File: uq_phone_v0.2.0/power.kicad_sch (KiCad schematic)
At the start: 37 parts, among them J2 124018312112A, J3 BM03B-ACHSS-GAN-TF_LF__SN_, U1 TPS62162DSGR, U15 TPS22964CYZPR, U2 MCP73871-2CCI_ML, U3 BQ27441DRZR-G1A

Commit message: Restructure, route and add flex pcb
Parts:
- C1, C3: LCSC PN C2168196 -> C19702
- C5: LCSC PN C26412 -> C526993
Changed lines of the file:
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@@
 			)
 		)
-		(property "LCSC PN" "C26412"
+		(property "LCSC PN" "C526993"
 			(at 273.05 185.42 0)
 			(effects
@@
 			)
 		)
-		(property "LCSC PN" "C2168196"
+		(property "LCSC PN" "C19702"
 			(at 90.17 173.99 0)
 			(effects
@@
 			)
 		)
-		(property "LCSC PN" "C2168196"
+		(property "LCSC PN" "C19702"
 			(at 213.36 59.69 0)
 			(effects

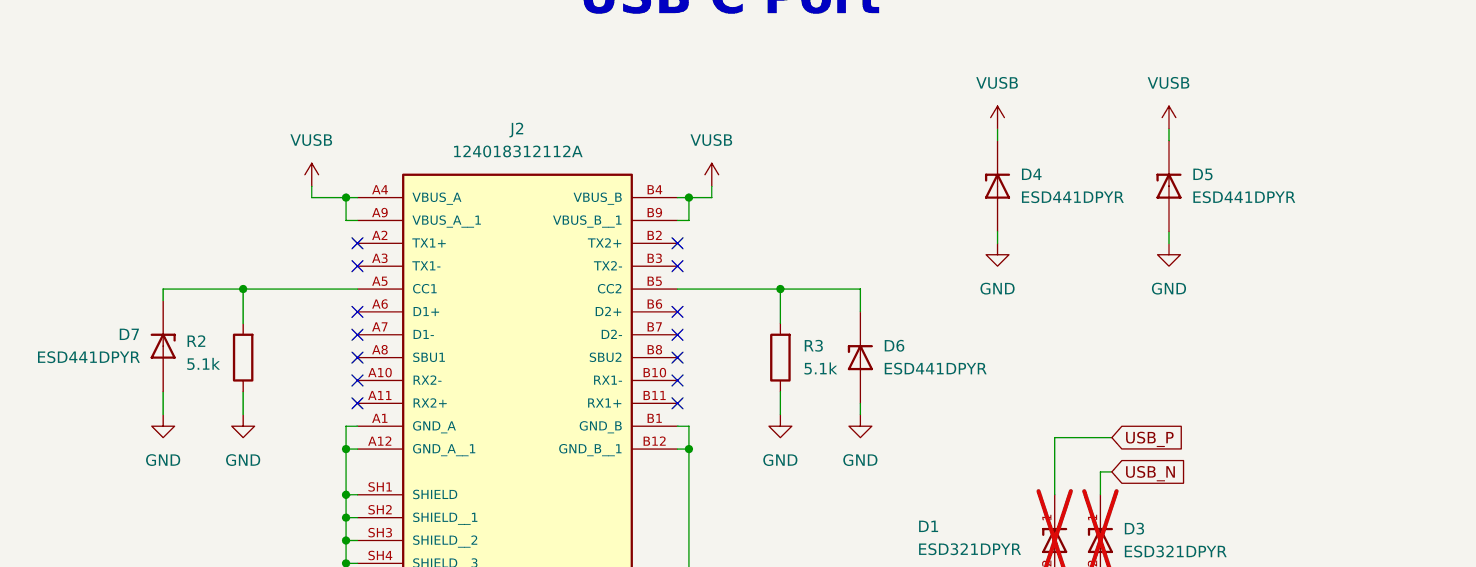
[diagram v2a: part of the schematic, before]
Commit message: Add GNSS antenna for sag
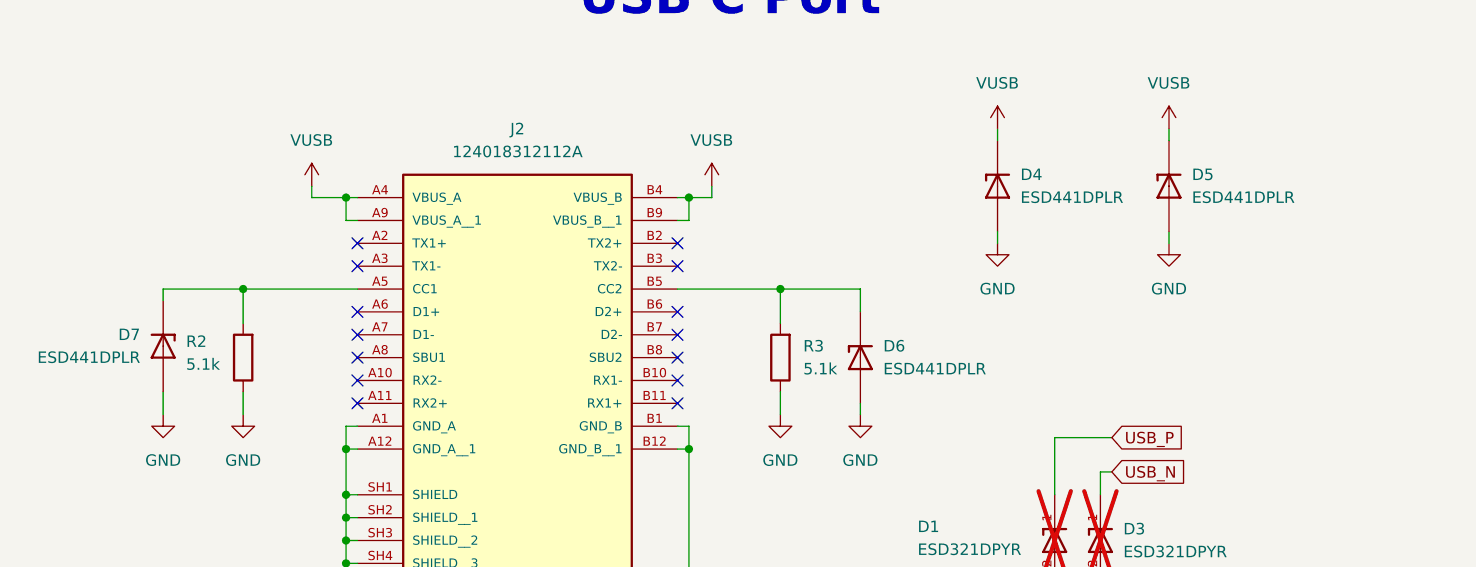
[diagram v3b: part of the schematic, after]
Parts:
- D4, D5, D6, D7: value ESD441DPYR -> ESD441DPLR
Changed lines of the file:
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@@
 			)
 		)
-		(property "Value" "ESD441DPYR"
+		(property "Value" "ESD441DPLR"
 			(at 124.46 43.1799 90)
 			(effects
@@
 			)
 		)
-		(property "Value" "ESD441DPYR"
+		(property "Value" "ESD441DPLR"
 			(at 109.22 62.2299 90)
 			(effects
@@
 			)
 		)
-		(property "Value" "ESD441DPYR"
+		(property "Value" "ESD441DPLR"
 			(at 143.51 43.1799 90)
 			(effects
@@
 			)
 		)
-		(property "Value" "ESD441DPYR"
+		(property "Value" "ESD441DPLR"
 			(at 26.67 60.9599 90)
 			(effects

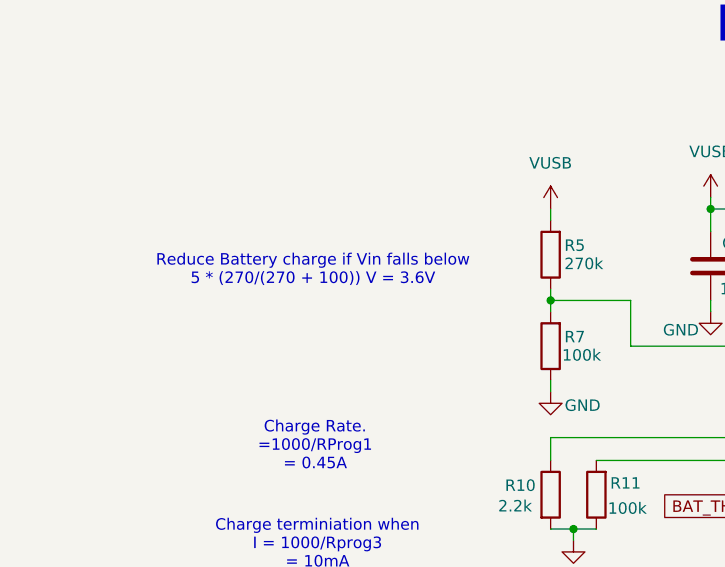
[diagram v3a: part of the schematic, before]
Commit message: Fixed display pinout
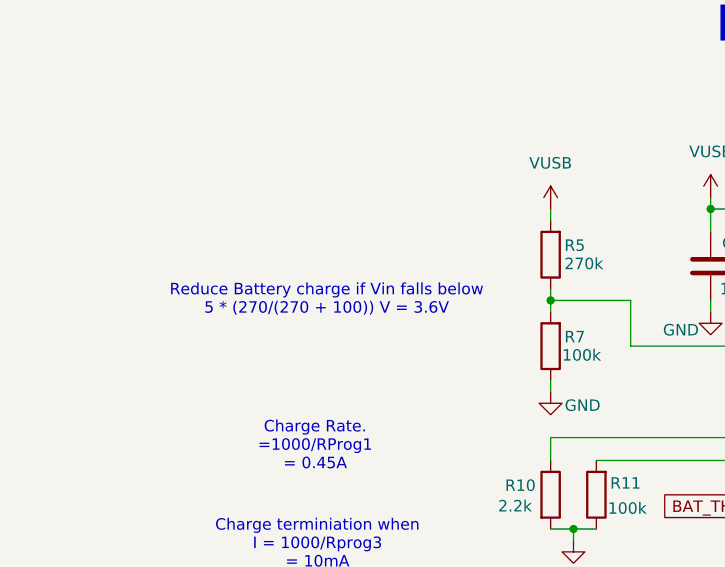
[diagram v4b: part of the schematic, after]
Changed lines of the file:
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@@
 	(text "Reduce Battery charge if Vin falls below\n5 * (270/(270 + 100)) V = 3.6V"
 		(exclude_from_sim no)
-		(at 45.974 174.498 0)
+		(at 47.498 177.8 0)
 		(effects
 			(font

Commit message: Cleaning up adn fixing massive mistake
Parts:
- B1: value 113450 -> 414360
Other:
- note added: "Charge Rate = 1000/RProg1 = 0.45A"
- note added: "Charge Termination Current = 1000/Rprog3 = 10mA"
- note added: "Reduce battery charge if IN falls below VPCC = 3.6V"
- note added: "UQ Phone"
- note removed: "Battery Manager"
- note removed: "Charge Rate. =1000/RProg1 = 0.45A"
- note removed: "Charge terminiation when I = 1000/Rprog3 = 10mA"
- note removed: "Fuel Gauge"
- note removed: "Internal Load switch"
- note removed: "Load Switch"
- note removed: "Only include if data lines are to go somewhere"
- note removed: "Reduce Battery charge if Vin falls below 5 * (270/(270 + 100)) V = 3.6V"
- note removed: "Test Points"
- note removed: "USB C Port"
- note removed: "Voltate Regulation"
- title: UQ Phone -> Power System
- moved on the sheet: B1, C1, C2, C3, C30, C31, C4, C5, C6, C7, D1, D3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

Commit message: minor comments
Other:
- note added: "Need to add soft power switch"
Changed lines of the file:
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@@
+		)
+	)
+	(text "Need to add soft power switch "
+		(exclude_from_sim no)
+		(at 331.978 221.996 0)
+		(effects
+			(font
+				(size 1.27 1.27)
+				(thickness 0.254)
+				(bold yes)
+				(color 255 0 0 1)
+			)
 		)
 	)
